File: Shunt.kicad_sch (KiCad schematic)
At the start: 1 part

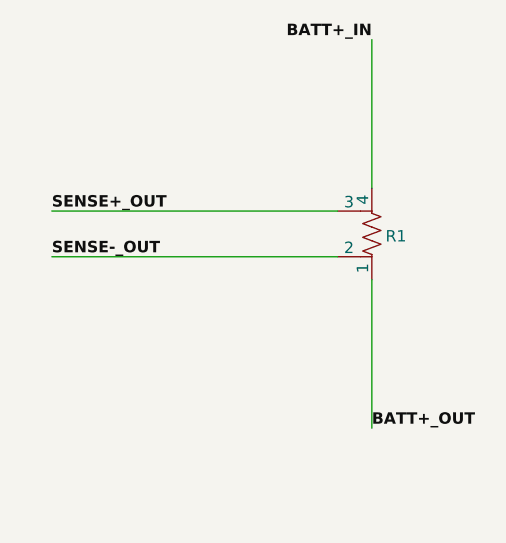
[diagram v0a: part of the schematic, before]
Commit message: Assigned footprints
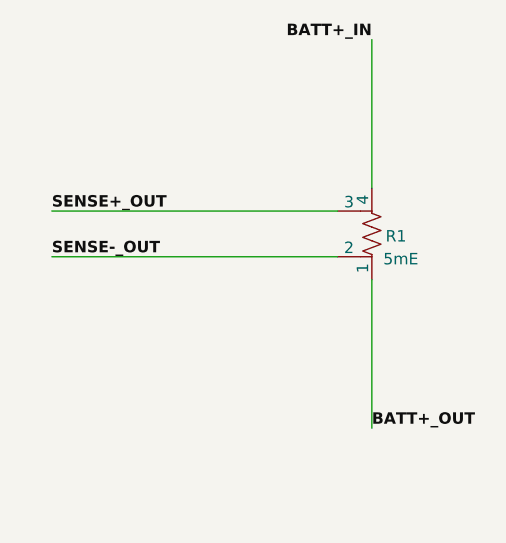
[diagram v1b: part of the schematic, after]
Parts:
- R1: value R_Shunt_US -> 5mE; footprint (none) -> PP_PoC:R_2512_6332Metric; Robu (none) -> 591923
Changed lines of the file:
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@@
 			)
 		)
-		(property "Value" "R_Shunt_US"
-			(at 160.02 106.6799 0)
+		(property "Value" "5mE"
+			(at 158.75 108.204 0)
 			(effects
 				(font
@@
 				)
 				(justify right)
-				(hide yes)
 			)
 		)
-		(property "Footprint" ""
+		(property "Footprint" "PP_PoC:R_2512_6332Metric"
 			(at 159.258 105.41 90)
 			(effects
@@
 			(at 157.48 105.41 0)
 			(effects
+				(font
+					(size 1.27 1.27)
+				)
+				(hide yes)
+			)
+		)
+		(property "Robu" "591923"
+			(at 157.48 105.41 0)
+			(effects

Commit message: Started routing
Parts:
- added C2: 100nF, PP_PoC:C_0603_1608Metric_Pad1.08x0.95mm_HandSolder, symbol PP_PoC:C
- added R5, R6: 100E, PP_PoC:R_0402_1005Metric_Pad0.72x0.64mm_HandSolder, symbol PP_PoC:R_US
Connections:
- net BATT+_IN is gone; now on net BATT+_OUT: R1.4
- net BATT+_OUT: no longer R1.1
- net SENSE+_OUT: now also C2.2, R5.1; no longer R1.3
- net SENSE-_OUT: now also C2.1, R6.1; no longer R1.2
- new net: R1.2, R6.2
- new net: R1.3, R5.2
- new net GND: R1.1
